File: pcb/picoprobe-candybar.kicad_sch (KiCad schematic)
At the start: 35 parts, among them J0 SWD-UART_PicoprobeCandybar, J1 PinHeader_2x04, J2 PinSocket_1x03, J3 PinSocket_1x03, J4 PinSocket_1x03, J5 PinSocket_1x03, J6 PinSocket_1x03, J7 PinSocket_1x03, Q1 T2N7002AK, Q2 DMP31D1U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

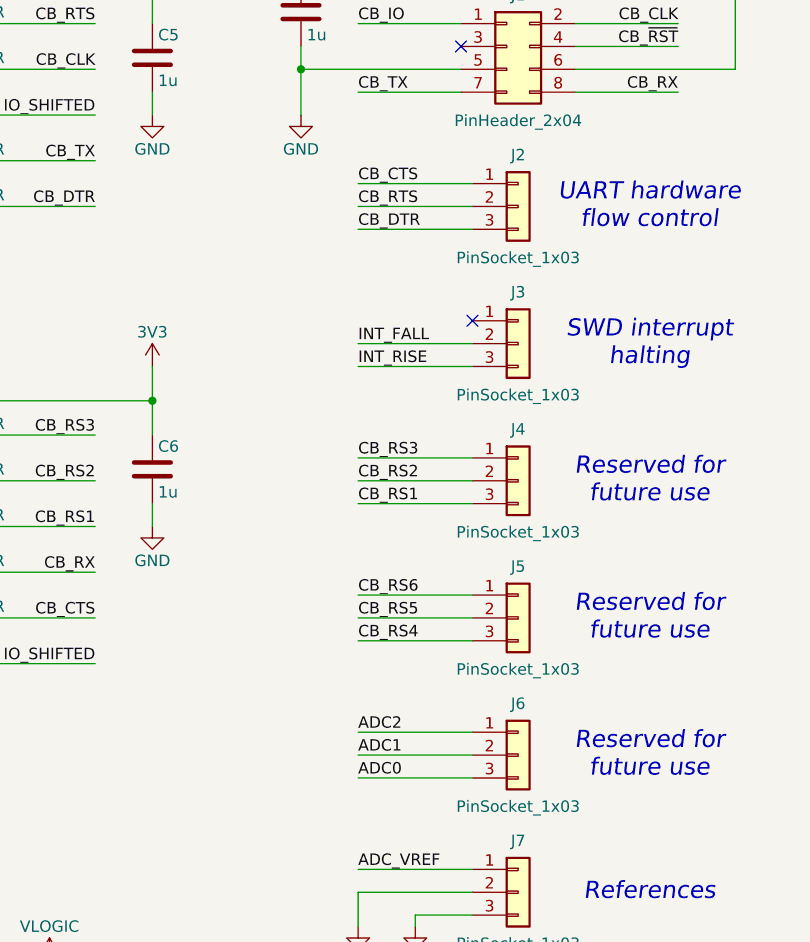
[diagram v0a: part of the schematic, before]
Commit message: Continue refining layout; add SMD PinHeader
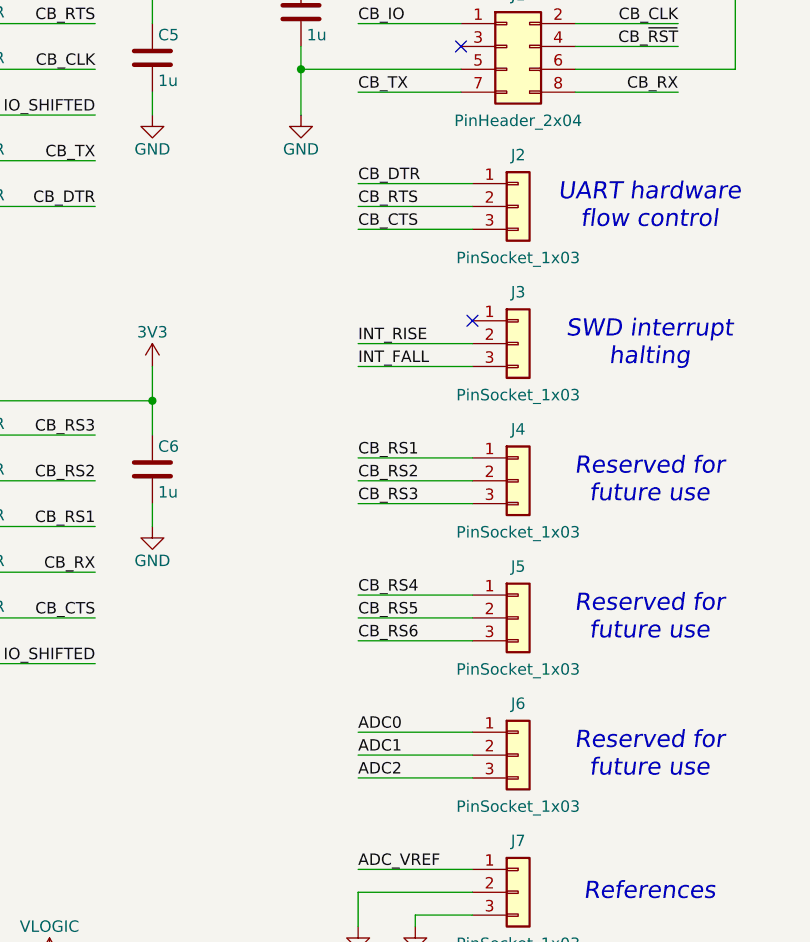
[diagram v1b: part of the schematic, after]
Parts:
- J2, J3, J4, J5, J6, J7: footprint Connector_PinSocket_2.54mm:PinSocket_1x03_P2.54mm_Vertical_SMD_Pin1Left -> ProjectFootprints_PicoprobeCandybar:PinHeader_1x03_P2.54mm_Horizontal_SMD
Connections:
- net ADC0: now also J6.1 (Pin_1); no longer J6.3 (Pin_3)
- net ADC2: now also J6.3 (Pin_3); no longer J6.1 (Pin_1)
- net CB_CTS: now also J2.3 (Pin_3); no longer J2.1 (Pin_1)
- net CB_DTR: now also J2.1 (Pin_1); no longer J2.3 (Pin_3)
- net CB_RS1: now also J4.1 (Pin_1); no longer J4.3 (Pin_3)
- net CB_RS3: now also J4.3 (Pin_3); no longer J4.1 (Pin_1)
- net CB_RS4: now also J5.1 (Pin_1); no longer J5.3 (Pin_3)
- net CB_RS6: now also J5.3 (Pin_3); no longer J5.1 (Pin_1)
- net INT_FALL: now also J3.3 (Pin_3); no longer J3.2 (Pin_2)
- net INT_RISE: now also J3.2 (Pin_2); no longer J3.3 (Pin_3)
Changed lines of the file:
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@@
 	(wire
 		(pts
-			(xy 228.6 76.2) (xy 241.3 76.2)
-		)
-		(stroke
-			(width 0)
-			(type default)
-		)
-	)
-	(wire
-		(pts
 			(xy 148.59 152.4) (xy 148.59 153.67)
 		)
@@
 	(wire
 		(pts
-			(xy 229.87 166.37) (xy 242.57 166.37)
+			(xy 228.6 73.66) (xy 241.3 73.66)
 		)
 		(stroke
@@
 	(wire
 		(pts
-			(xy 116.84 87.63) (xy 127 87.63)
+			(xy 229.87 166.37) (xy 242.57 166.37)
 		)
 		(stroke
@@
 	(wire
 		(pts
-			(xy 116.84 90.17) (xy 127 90.17)
+			(xy 116.84 87.63) (xy 127 87.63)
 		)
 		(stroke
@@
 	(wire
 		(pts
-			(xy 252.73 153.67) (xy 252.73 161.29)
+			(xy 116.84 90.17) (xy 127 90.17)
 		)
 		(stroke
@@
 	(wire
 		(pts
-			(xy 147.32 151.13) (xy 148.59 151.13)
+			(xy 252.73 153.67) (xy 252.73 161.29)
 		)
 		(stroke
@@
 	(wire
 		(pts
-			(xy 228.6 73.66) (xy 241.3 73.66)
+			(xy 147.32 151.13) (xy 148.59 151.13)
 		)
 		(stroke
@@
 	(wire
 		(pts
+			(xy 228.6 76.2) (xy 241.3 76.2)
+		)
+		(stroke
+			(width 0)
+			(type default)
+		)
+	)
+	(wire
+		(pts
 			(xy 270.51 43.18) (xy 252.73 43.18)
 		)
@@
 		)
 	)
-	(label "CB_RS6"
-		(at 228.6 101.6 0)
-		(fields_autoplaced yes)
-		(effects
-			(font
-				(size 1.27 1.27)
-			)
-			(justify left bottom)
-		)
-	)
 	(label "CB_RTS"
 		(at 228.6 58.42 0)
@@
 		)
 	)
-	(label "ADC0"
-		(at 228.6 121.92 0)
-		(fields_autoplaced yes)
-		(effects
-			(font
-				(size 1.27 1.27)
-			)
-			(justify left bottom)
-		)
-	)
 	(label "INT_FALL"
 		(at 60.96 80.01 0)
@@
 		)
 	)
-	(label "RS2"
-		(at 139.7 88.9 0)
+	(label "CB_RS3"
+		(at 228.6 91.44 0)
 		(fields_autoplaced yes)
 		(effects
@@
 		)
 	)
-	(label "CB_RX"
-		(at 264.16 45.72 180)
+	(label "ADC0"
+		(at 228.6 116.84 0)
 		(fields_autoplaced yes)
 		(effects
@@
 				(size 1.27 1.27)
 			)
-			(justify right bottom)
+			(justify left bottom)
 		)
 	)
-	(label "CB_RS5"
-		(at 228.6 104.14 0)
+	(label "RS2"
+		(at 139.7 88.9 0)
 		(fields_autoplaced yes)
 		(effects
@@
 		)
 	)
-	(label "CB_CTS"
-		(at 228.6 55.88 0)
+	(label "CB_RX"
+		(at 264.16 45.72 180)
+		(fields_autoplaced yes)
+		(effects
+			(font
+				(size 1.27 1.27)
+			)
+			(justify right bottom)
+		)
+	)
+	(label "CB_RS5"
+		(at 228.6 104.14 0)
 		(fields_autoplaced yes)
 		(effects
@@
 		)
 	)
-	(label "CB_DTR"
-		(at 228.6 60.96 0)
+	(label "CB_RS2"
+		(at 199.39 88.9 180)
 		(fields_autoplaced yes)
 		(effects
@@
 				(size 1.27 1.27)
 			)
-			(justify left bottom)
+			(justify right bottom)
 		)
 	)
-	(label "CB_RS2"
-		(at 199.39 88.9 180)
+	(label "CB_DTR"
+		(at 228.6 55.88 0)
 		(fields_autoplaced yes)
 		(effects
@@
 				(size 1.27 1.27)
 			)
-			(justify right bottom)
+			(justify left bottom)
 		)
 	)
@@
 		)
 	)
-	(label "ADC2"
-		(at 228.6 116.84 0)
+	(label "CB_RS6"
+		(at 228.6 106.68 0)
 		(fields_autoplaced yes)
 		(effects
@@
 		)
 	)
-	(label "CB_RS3"
-		(at 228.6 86.36 0)
+	(label "CB_CTS"
+		(at 228.6 60.96 0)
 		(fields_autoplaced yes)
 		(effects
@@
 		)
 	)
-	(label "INT_RISE"
-		(at 228.6 76.2 0)
-		(fields_autoplaced yes)
-		(effects
-			(font
-				(size 1.27 1.27)
-			)
-			(justify left bottom)
-		)
-	)
 	(label "IO_SHIFTED"
 		(at 139.7 132.08 0)
@@
 		)
 	)
+	(label "ADC2"
+		(at 228.6 121.92 0)
+		(fields_autoplaced yes)
+		(effects
+			(font
+				(size 1.27 1.27)
+			)
+			(justify left bottom)
+		)
+	)
 	(label "RTS"
 		(at 60.96 69.85 0)
@@
 	)
 	(label "INT_FALL"
-		(at 228.6 73.66 0)
+		(at 228.6 76.2 0)
 		(fields_autoplaced yes)
 		(effects
@@
 		)
 	)
-	(label "CB_RS4"
-		(at 228.6 106.68 0)
+	(label "INT_RISE"
+		(at 228.6 73.66 0)
 		(fields_autoplaced yes)
 		(effects
@@
 		)
 	)
-	(label "CB_RS1"
-		(at 228.6 91.44 0)
-		(fields_autoplaced yes)
-		(effects
-			(font
-				(size 1.27 1.27)
-			)
-			(justify left bottom)
-		)
-	)
 	(label "CLK"
 		(at 139.7 43.18 0)
@@
 		)
 	)
+	(label "CB_RS4"
+		(at 228.6 101.6 0)
+		(fields_autoplaced yes)
+		(effects
+			(font
+				(size 1.27 1.27)
+			)
+			(justify left bottom)
+		)
+	)
+	(label "CB_RS1"
+		(at 228.6 86.36 0)
+		(fields_autoplaced yes)
+		(effects
+			(font
+				(size 1.27 1.27)
+			)
+			(justify left bottom)
+		)
+	)
 	(label "LED_RUN"
 		(at 127 59.69 180)
@@
 			)
 		)
-		(property "Footprint" "Connector_PinSocket_2.54mm:PinSocket_1x03_P2.54mm_Vertical_SMD_Pin1Left"
+		(property "Footprint" "ProjectFootprints_PicoprobeCandybar:PinHeader_1x03_P2.54mm_Horizontal_SMD"
 			(at 246.38 134.62 0)
 			(effects
@@
 			)
 		)
-		(property "Footprint" "Connector_PinSocket_2.54mm:PinSocket_1x03_P2.54mm_Vertical_SMD_Pin1Left"
+		(property "Footprint" "ProjectFootprints_PicoprobeCandybar:PinHeader_1x03_P2.54mm_Horizontal_SMD"
 			(at 246.38 58.42 0)
 			(effects
@@
 			)
 		)
-		(property "Footprint" "Connector_PinSocket_2.54mm:PinSocket_1x03_P2.54mm_Vertical_SMD_Pin1Left"
+		(property "Footprint" "ProjectFootprints_PicoprobeCandybar:PinHeader_1x03_P2.54mm_Horizontal_SMD"
 			(at 246.38 104.14 0)
 			(effects
@@
 			)
 		)
-		(property "Footprint" "Connector_PinSocket_2.54mm:PinSocket_1x03_P2.54mm_Vertical_SMD_Pin1Left"
+		(property "Footprint" "ProjectFootprints_PicoprobeCandybar:PinHeader_1x03_P2.54mm_Horizontal_SMD"
 			(at 246.38 73.66 0)
 			(effects
@@
 			)
 		)
-		(property "Footprint" "Connector_PinSocket_2.54mm:PinSocket_1x03_P2.54mm_Vertical_SMD_Pin1Left"
+		(property "Footprint" "ProjectFootprints_PicoprobeCandybar:PinHeader_1x03_P2.54mm_Horizontal_SMD"
 			(at 246.38 88.9 0)
 			(effects
@@
 			)
 		)
-		(property "Footprint" "Connector_PinSocket_2.54mm:PinSocket_1x03_P2.54mm_Vertical_SMD_Pin1Left"
+		(property "Footprint" "ProjectFootprints_PicoprobeCandybar:PinHeader_1x03_P2.54mm_Horizontal_SMD"
 			(at 246.38 119.38 0)
 			(effects

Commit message: Update candybar-interface to 'swd-only' HEAD
Reorders `RST`, `GND`, and `VCC`.
Needed in order to bring Candybar layout to parity.
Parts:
- J0: footprint Connector_PicoprobeCandybar:SWD-UART_PicoprobeCandybar_2Rows_7Pins_P2.54mm_Polarized_PressFit_Vertical -> SWD-UART_PicoprobeCandybar_PressFit
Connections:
- net 3V3_EN: now also J0.6 (~{RESET}); no longer J0.4 (~{RESET})
- net GND: now also J0.3 (GND); no longer J0.5 (GND)
- net VSYS: now also J0.4 (VCC); no longer J0.6 (VCC)
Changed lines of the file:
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@@
 			)
 		)
-		(property "Footprint" "Connector_PicoprobeCandybar:SWD-UART_PicoprobeCandybar_2Rows_7Pins_P2.54mm_Polarized_PressFit_Vertical"
+		(property "Footprint" "SWD-UART_PicoprobeCandybar_PressFit"
 			(at 39.37 76.2 0)
 			(effects
@@
 			)
 		)
-		(property "Description" "A zero-cost press-fit debug interface for the Picoprobe Candybar debug probe, SWD, power, UART, ARM, Cortex"
+		(property "Description" "A zero-cost press-fit debug interface for the Picoprobe Candybar debug probe, providing SWD, power, and UART"
 			(at 39.37 81.28 0)
 			(effects
@@
 		(pin "6"
 		)
-		(pin "5"
+		(pin "3"
 		)
 		(pin "7"

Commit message: Update DEBUG OUT pinout
Also fixes candybar-interface footprint name
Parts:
- J0: footprint SWD-UART_PicoprobeCandybar_PressFit -> Connector_PicoprobeCandybar:SWD-UART_PicoprobeCandybar_PressFit
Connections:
- net CB_~{RST}: now also J1.6 (Pin_6); no longer J1.4 (Pin_4)
- net GND: now also J1.3 (Pin_3); no longer J1.5 (Pin_5)
- net VOUT: now also J1.4 (Pin_4); no longer J1.6 (Pin_6)
- no-connect marks 5 -> 4
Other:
- moved on the sheet: C7
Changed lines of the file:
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@@
 	)
 	(junction
-		(at 222.25 43.18)
-		(diameter 0)
-		(color 0 0 0 0)
-	)
-	(junction
 		(at 43.18 163.83)
 		(diameter 0)
@@
 	)
 	(junction
+		(at 222.25 40.64)
+		(diameter 0)
+		(color 0 0 0 0)
+	)
+	(junction
 		(at 205.74 34.29)
 		(diameter 0)
@@
 	)
 	(no_connect
-		(at 240.03 40.64)
-	)
-	(no_connect
 		(at 71.12 95.25)
 	)
@@
 	(wire
 		(pts
+			(xy 264.16 43.18) (xy 252.73 43.18)
+		)
+		(stroke
+			(width 0)
+			(type default)
+		)
+	)
+	(wire
+		(pts
 			(xy 48.26 151.13) (xy 48.26 153.67)
 		)
@@
 	(wire
 		(pts
-			(xy 270.51 30.48) (xy 270.51 43.18)
+			(xy 270.51 30.48) (xy 270.51 40.64)
 		)
 		(stroke
@@
 	(wire
 		(pts
+			(xy 222.25 40.64) (xy 240.03 40.64)
+		)
+		(stroke
+			(width 0)
+			(type default)
+		)
+	)
+	(wire
+		(pts
 			(xy 241.3 137.16) (xy 234.95 137.16)
 		)
@@
 	(wire
 		(pts
+			(xy 222.25 39.37) (xy 222.25 40.64)
+		)
+		(stroke
+			(width 0)
+			(type default)
+		)
+	)
+	(wire
+		(pts
 			(xy 116.84 67.31) (xy 127 67.31)
 		)
@@
 	(wire
 		(pts
+			(xy 270.51 40.64) (xy 252.73 40.64)
+		)
+		(stroke
+			(width 0)
+			(type default)
+		)
+	)
+	(wire
+		(pts
 			(xy 170.18 43.18) (xy 177.8 43.18)
 		)
@@
 	(wire
 		(pts
-			(xy 222.25 43.18) (xy 222.25 48.26)
+			(xy 222.25 40.64) (xy 222.25 48.26)
 		)
 		(stroke
@@
 	(wire
 		(pts
-			(xy 222.25 40.64) (xy 222.25 43.18)
-		)
-		(stroke
-			(width 0)
-			(type default)
-		)
-	)
-	(wire
-		(pts
 			(xy 228.6 73.66) (xy 241.3 73.66)
 		)
@@
 	(wire
 		(pts
-			(xy 222.25 43.18) (xy 240.03 43.18)
-		)
-		(stroke
-			(width 0)
-			(type default)
-		)
-	)
-	(wire
-		(pts
 			(xy 207.01 153.67) (xy 222.25 153.67)
 		)
@@
 	(wire
 		(pts
-			(xy 270.51 43.18) (xy 252.73 43.18)
-		)
-		(stroke
-			(width 0)
-			(type default)
-		)
-	)
-	(wire
-		(pts
 			(xy 45.72 110.49) (xy 53.34 110.49)
 		)
@@
 	(wire
 		(pts
-			(xy 264.16 40.64) (xy 252.73 40.64)
-		)
-		(stroke
-			(width 0)
-			(type default)
-		)
-	)
-	(wire
-		(pts
 			(xy 49.53 59.69) (xy 50.8 59.69)
 		)
@@
 	(wire
 		(pts
-			(xy 222.25 30.48) (xy 222.25 33.02)
+			(xy 222.25 30.48) (xy 222.25 31.75)
 		)
 		(stroke
@@
 		)
 	)
-	(label "CB_~{RST}"
-		(at 264.16 40.64 180)
-		(fields_autoplaced yes)
-		(effects
-			(font
-				(size 1.27 1.27)
-			)
-			(justify right bottom)
-		)
-	)
 	(label "LED_CON"
 		(at 60.96 90.17 0)
@@
 		)
 	)
+	(label "CB_~{RST}"
+		(at 264.16 43.18 180)
+		(fields_autoplaced yes)
+		(effects
+			(font
+				(size 1.27 1.27)
+			)
+			(justify right bottom)
+		)
+	)
 	(label "CB_RS1"
 		(at 228.6 86.36 0)
@@
 	(symbol
 		(lib_id "Device:C")
-		(at 222.25 36.83 0)
+		(at 222.25 35.56 0)
 		(unit 1)
 		(exclude_from_sim no)
@@
 		(dnp no)
 		(property "Reference" "C7"
-			(at 222.885 34.29 0)
+			(at 222.885 33.02 0)
 			(effects
 				(font
@@
 		)
 		(property "Value" "1u"
-			(at 222.885 39.37 0)
+			(at 222.885 38.1 0)
 			(effects
 				(font
@@
 		)
 		(property "Footprint" "Capacitor_SMD:C_0805_2012Metric_Pad1.18x1.45mm_HandSolder"
-			(at 223.2152 40.64 0)
+			(at 223.2152 39.37 0)
 			(effects
 				(font
@@
 		)
 		(property "Datasheet" "~"
-			(at 222.25 36.83 0)
+			(at 222.25 35.56 0)
 			(effects
 				(font
@@
 		)
 		(property "Description" "Unpolarized capacitor"
-			(at 222.25 36.83 0)
+			(at 222.25 35.56 0)
 			(effects
 				(font
@@
 		(pin "8"
 		)
-		(pin "5"
-		)
 		(pin "1"
 		)
@@
 			)
 		)
-		(property "Footprint" "SWD-UART_PicoprobeCandybar_PressFit"
+		(property "Footprint" "Connector_PicoprobeCandybar:SWD-UART_PicoprobeCandybar_PressFit"
 			(at 39.37 76.2 0)
 			(effects

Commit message: Use compact interface for DEBUG IN
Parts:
- J0: footprint Connector_PicoprobeCandybar:SWD-UART_PicoprobeCandybar_PressFit -> Connector_PicoprobeCandybar:SWD-UART_PicoprobeCandybar_PressFit_Compact
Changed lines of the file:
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@@
 			)
 		)
-		(property "Footprint" "Connector_PicoprobeCandybar:SWD-UART_PicoprobeCandybar_PressFit"
+		(property "Footprint" "Connector_PicoprobeCandybar:SWD-UART_PicoprobeCandybar_PressFit_Compact"
 			(at 39.37 76.2 0)
 			(effects

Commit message: Change Q2 out for an available alternative
Original DMP31D1U was on backorder on Digi-Key.
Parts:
- Q2: value DMP31D1U -> GSFC02501
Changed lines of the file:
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@@
 			)
 		)
-		(property "Value" "DMP31D1U"
+		(property "Value" "GSFC02501"
 			(at 97.79 157.48 0)
 			(effects
@@
 			)
 		)
-		(property "Datasheet" "https://www.diodes.com/assets/Datasheets/DMP31D1U.pdf"
+		(property "Datasheet" "https://goodarksemi.com/docs/datasheets/mosfets/GSFC02501.pdf"
 			(at 92.71 158.75 0)
 			(effects

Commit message: Update side output names to "PinHeader_1x03"
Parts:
- J2, J3, J4, J5, J6, J7: value PinSocket_1x03 -> PinHeader_1x03
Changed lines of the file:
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@@
 			)
 		)
-		(property "Value" "PinSocket_1x03"
+		(property "Value" "PinHeader_1x03"
 			(at 246.38 140.335 0)
 			(effects
@@
 			)
 		)
-		(property "Value" "PinSocket_1x03"
+		(property "Value" "PinHeader_1x03"
 			(at 246.38 64.135 0)
 			(effects
@@
 			)
 		)
-		(property "Value" "PinSocket_1x03"
+		(property "Value" "PinHeader_1x03"
 			(at 246.38 109.855 0)
 			(effects
@@
 			)
 		)
-		(property "Value" "PinSocket_1x03"
+		(property "Value" "PinHeader_1x03"
 			(at 246.38 79.375 0)
 			(effects
@@
 			)
 		)
-		(property "Value" "PinSocket_1x03"
+		(property "Value" "PinHeader_1x03"
 			(at 246.38 94.615 0)
 			(effects
@@
 			)
 		)
-		(property "Value" "PinSocket_1x03"
+		(property "Value" "PinHeader_1x03"
 			(at 246.38 125.095 0)
 			(effects

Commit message: Change Q1 out for a cheaper alternative
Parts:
- Q1: value T2N7002AK -> SSF2320Y
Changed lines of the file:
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@@
 			)
 		)
-		(property "Value" "T2N7002AK"
+		(property "Value" "SSF2320Y"
 			(at 85.09 171.45 0)
 			(effects
@@
 			)
 		)
-		(property "Datasheet" "https://toshiba.semicon-storage.com/info/T2N7002AK_datasheet_en_20150401.pdf"
+		(property "Datasheet" "https://goodarksemi.com/docs/datasheets/mosfets/SSF2320Y.pdf"
 			(at 80.01 171.45 0)
 			(effects

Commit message: Add Manufacturer & Product Number entries for BOM
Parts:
- A1: Manufacturer (none) -> Raspberry Pi; Manufacturer Part Number (none) -> SC0915
- D1: Manufacturer (none) -> Nexperia USA Inc.; Manufacturer Part Number (none) -> PMEG2010ER
- D2: Manufacturer (none) -> ams-OSRAM USA INC.; Manufacturer Part Number (none) -> LO R976-PS-1-0-20-R18
- D3: Manufacturer (none) -> ams-OSRAM USA INC.; Manufacturer Part Number (none) -> LY R976-PS-36-0-20-R18
- D4: Manufacturer (none) -> ams-OSRAM USA INC.; Manufacturer Part Number (none) -> LG R971-KN-1-0-20-R18
- D5: Manufacturer (none) -> ams-OSRAM USA INC.; Manufacturer Part Number (none) -> LS R976-NR-1-0-20-R18
- Q1: Manufacturer (none) -> Good-Ark Semiconductor; Manufacturer Part Number (none) -> SSF2320Y
- Q2: Manufacturer (none) -> Good-Ark Semiconductor; Manufacturer Part Number (none) -> GSFC02501
- SW1: Manufacturer (none) -> Adam Tech; Manufacturer Part Number (none) -> SW-R1-1A-E-1-0
- SW2: Manufacturer (none) -> Same Sky; Manufacturer Part Number (none) -> SLW-156646-5A-N-D
- SW3: Manufacturer (none) -> Same Sky; Manufacturer Part Number (none) -> SLW-1277545-2A-RA-S-D
- U1: Manufacturer (none) -> Texas Instruments; Manufacturer Part Number (none) -> TLV77318PDBVR
- U2: Manufacturer (none) -> Texas Instruments; Manufacturer Part Number (none) -> TLV77325PDBVR
- U3, U4: Manufacturer (none) -> Texas Instruments; Manufacturer Part Number (none) -> SN74LV6T17
